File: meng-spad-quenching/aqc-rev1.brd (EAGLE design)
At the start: 127 x 88.9 mm, 138 parts, among them IC1 ADCMP582, IC2 NC7SV74K8X, IC3 LT3032-5, IC4 OPA342, IC5 OPA342, IC6 LTC1711, IC7 DS1100LU-20+, IC8 LT3032-15, IC9 NC7WZ16P6X, J1 VIN_LOGIC, M1 BSS806N, Q1 MMBTH81, Q2 MMBTH81, Q3 MMBTH81, Q4 MMBTH81, Q5 MMBTH81, Q6 MMBTH81, SW1 CJS-1200TB, SW2 CJS-1200TB, SW3 CJS-1200TB, T1 MMBTH10, T2 MMBTH10, T3 MMBTH10, T4 MMBTH10, T5 MMBTH10, T6 MMBTH10, T7 MMBTH10, U1 SN65EPT21DGK, U2 TPS78233DDCT, U3 SN65EPT22DGK, X1 CONN_SPAD, X2 CONN_PHOTON_COUNTER, X3 CONN_FORCE_QUENCH, X4 CONN_VREF_ONE_SHOT_EXT, X5 CONN_VREF_DIAMOND_IBIAS_EXT, X6 CONN_VREF_CASCODE_IBIAS_EXT

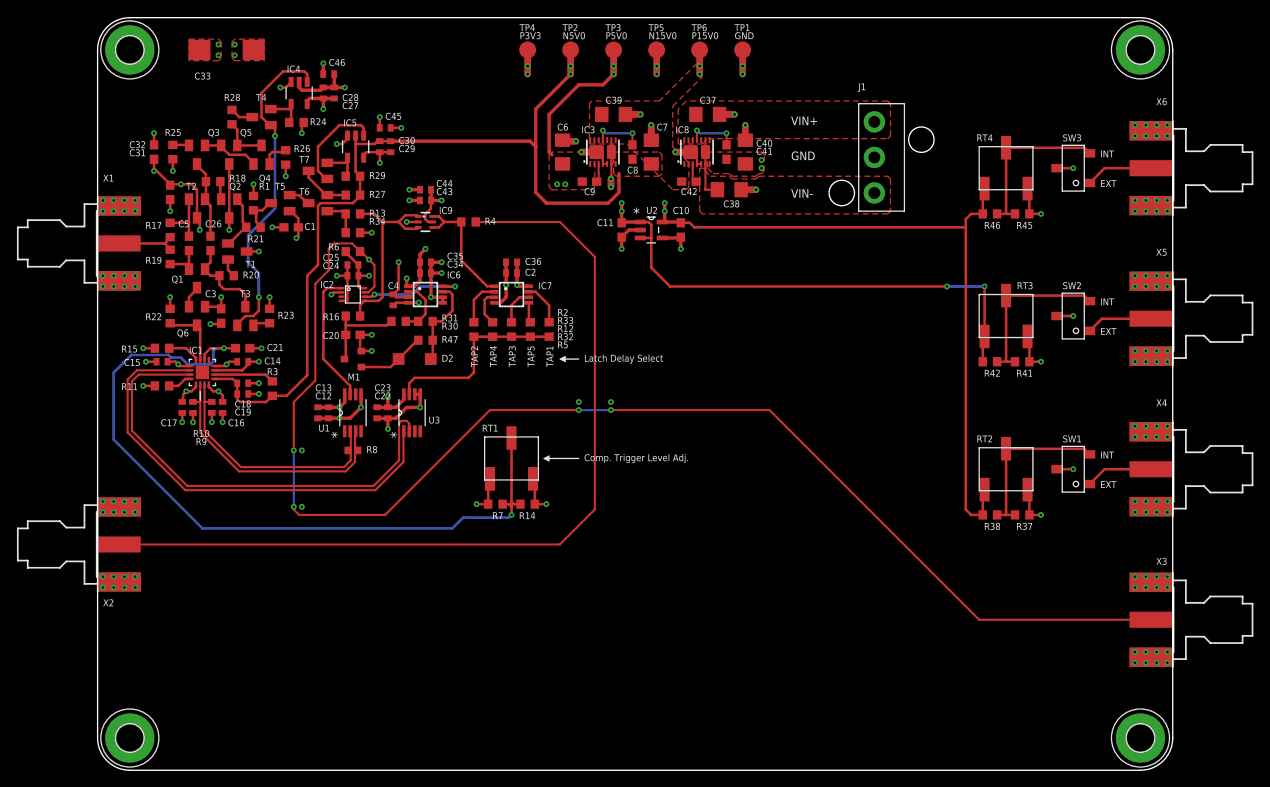
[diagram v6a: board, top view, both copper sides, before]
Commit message: Added VREF testpts, routed, exported gerbers
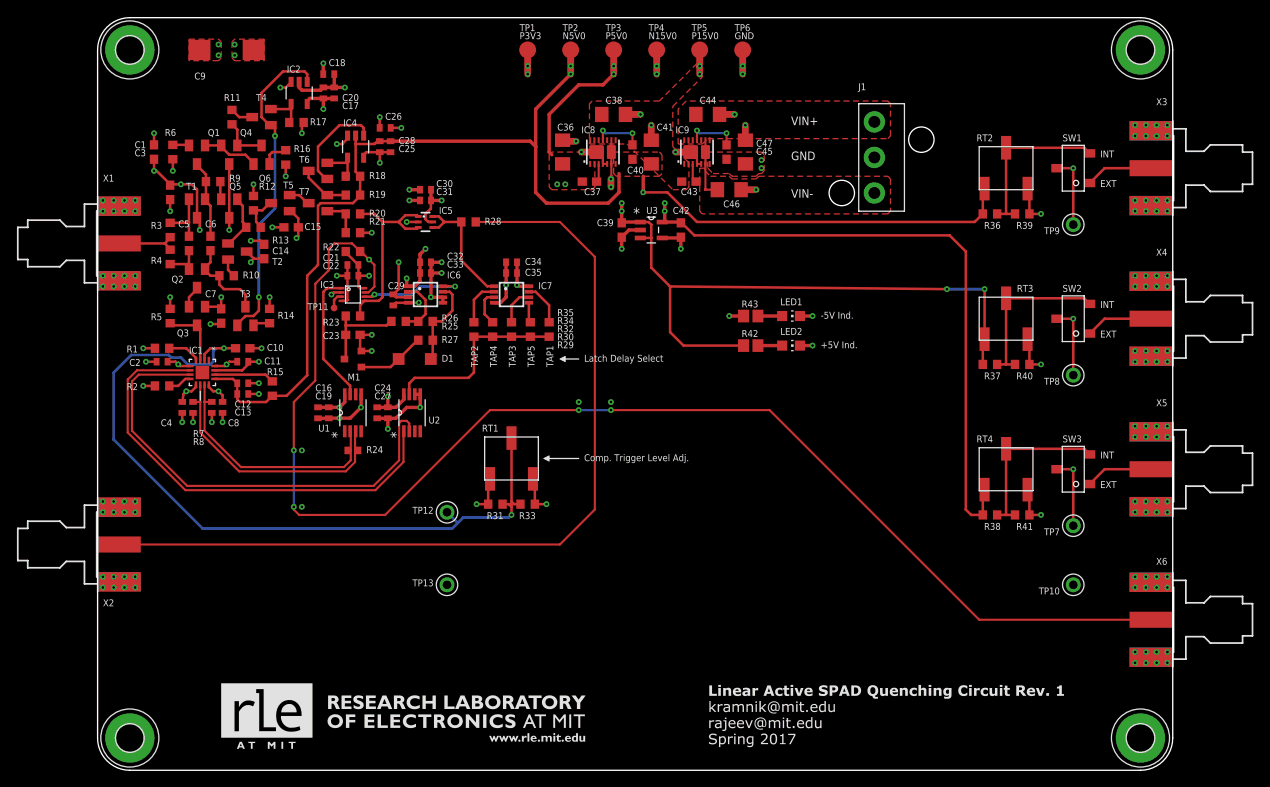
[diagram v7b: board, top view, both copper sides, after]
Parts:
- removed R47: 49R9, rcl:R0603
- added C47: 10u, rcl:C1206
- added LED1, LED2: (no value), led:CHIP-LED0805
- added R35, R40: DNP, rcl:R0603
- added R43: 470R, resistor:R0805
- added TP10, TP13: GND, Kramnik's Library:KEYSTONE_5000_MINIATURE
- added TP11: TPTP08R, testpad:TP08R
- added TP12: VREF_AV_DET, Kramnik's Library:KEYSTONE_5000_MINIATURE
- added TP7: VREF_ONE_SHOT, Kramnik's Library:KEYSTONE_5000_MINIATURE
- added TP8: VREF_DIAMOND_IBIAS, Kramnik's Library:KEYSTONE_5000_MINIATURE
- added TP9: VREF_CASCODE_IBIAS, Kramnik's Library:KEYSTONE_5000_MINIATURE
- C10, C16, C18, C25, C3, C35: value 100n -> 10n
- C11, C26, C31, C32: device rcl:C0603 -> rcl:C0402
- C14, C43, C45: device rcl:C0402 -> rcl:C0603
- C15: value 10n -> 100n; device rcl:C0402 -> rcl:C0603
- C19, C24, C34, C42: value 10n -> 100n
- C20: value 1n -> 100n; device rcl:C0603 -> rcl:C0402
- C21, C8: value 10n -> 100n; device rcl:C0603 -> rcl:C0402
- C23: value 100n -> 1n; device rcl:C0402 -> rcl:C0603
- C33: value 33u, 25V -> 10n; device rcl:CT7343 -> rcl:C0402
- C36, C44: value 100n -> 10u; device rcl:C0402 -> rcl:C1206
- C37, C40, C6: value 10u -> 10n; device rcl:C1206 -> rcl:C0603
- C39, C7: value 10u -> 100n; device rcl:C1206 -> rcl:C0603
- C41: value 10n -> 10u; device rcl:C0603 -> rcl:C1206
- C46: value 10n -> 10u; device rcl:C0402 -> rcl:C1206
- C9: value 10n -> 33u, 25V; device rcl:C0603 -> rcl:CT7343
- IC2: value NC7SV74K8X -> OPA342; device meng:US8_3.1MM_JDEC_MO-187 -> meng:SOT23-5
- IC3: value LT3032-5 -> NC7SV74K8X; device meng:DFN14-4X3DE -> meng:US8_3.1MM_JDEC_MO-187
- IC5: value OPA342 -> NC7WZ16P6X; device meng:SOT23-5 -> meng:SC70-6L
- IC8: value LT3032-15 -> LT3032-5
- IC9: value NC7WZ16P6X -> LT3032-15; device meng:SC70-6L -> meng:DFN14-4X3DE
- R1, R29: value 470R -> DNP
- R10, R9: value 150R -> 49R9; device rcl:R0402 -> rcl:R0603
- R11: value 49R9 -> 1k43
- R12: value DNP -> 470R
- R13: value 0R -> 49R9
- R14, R5: value DNP -> 1k
- R15: value DNP -> 10k
- R16: value 470R -> 1k
- R17, R6: value 49R9 -> 1k
- R18, R19: value 49R9 -> 470R
- R2: value DNP -> 49R9
- R20: value 49R9 -> 0R
- R21: value 49R9 -> DNP
- R22: value 1k -> 49R9
- R23: value 1k -> 470R
- R24: value 1k -> 100R; device rcl:R0603 -> rcl:R0402
- R25: value 1k -> 100R
- R26: value 1k -> 10k
- R27: value 470R -> 49R9
- R28: value 1k43 -> 49R9
- R3: value 10k -> 49R9
- R30: value 100R -> DNP
- R31: value 10k -> DNP
- R42: value DNP -> 470R; device rcl:R0603 -> resistor:R0805
- R7: value DNP -> 150R; device rcl:R0603 -> rcl:R0402
- R8: value 100R -> 150R
- U2: value TPS78233DDCT -> SN65EPT22DGK; device Texas Instruments_By_element14_Batch_1 (2):SOT95P280X110-5N -> Texas Instruments_By_element14_Batch_1:SOP65P490X110-8N
- U3: value SN65EPT22DGK -> TPS78233DDCT; device Texas Instruments_By_element14_Batch_1:SOP65P490X110-8N -> Texas Instruments_By_element14_Batch_1 (2):SOT95P280X110-5N
- X3: value CONN_FORCE_QUENCH -> CONN_VREF_CASCODE_IBIAS_EXT
- X4: value CONN_VREF_ONE_SHOT_EXT -> CONN_VREF_DIAMOND_IBIAS_EXT
- X5: value CONN_VREF_DIAMOND_IBIAS_EXT -> CONN_VREF_ONE_SHOT_EXT
- X6: value CONN_VREF_CASCODE_IBIAS_EXT -> CONN_FORCE_QUENCH
- moved H2 144.4 mm to (3.81, 3.81)
- moved H3 119.4 mm to (123.2, 85.1)
- moved H1 81.3 mm to (3.81, 85.1)
- moved C8 57.0 mm to (14.8, 42.9)
- moved C7 54.4 mm to (14.6, 53.7), turned to 270 degrees
- moved C10 53.6 mm to (17.1, 49.8), turned to 0 degrees
- moved X3 53.3 mm to (127.0, 71.1)
- moved X6 53.3 mm to (127.0, 17.8)
- moved C46 49.2 mm to (74.6, 68.6)
- moved C11 47.4 mm to (17.1, 48.3), turned to 0 degrees
- moved R2 46.2 mm to (7.62, 45.4), turned to 180 degrees
- moved C9 45.6 mm to (15.2, 85.1)
- moved C6 43.0 mm to (13.3, 62.2), turned to 270 degrees
- moved C2 42.6 mm to (7.62, 48.3)
- moved C17 40.7 mm to (26.7, 80.0), turned to 90 degrees
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- renumbered D2 to D1, R45 to R39, R46 to R36
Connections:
- new net N$39: LED1.A, R43.1
- new net N$40: LED2.A, R42.1
- net !FORCE_QUENCH: now also IC3.7, R22.1, X6.1; no longer IC2.7, R6.1, X3.1
- net !ONE_SHOT_CLR: now also IC3.6; no longer IC2.6
- net BLANKING_LATCH_EN: now also R29.1, R30.1, R34.1, R35.1, U2.7; no longer R12.1, R2.1, R33.1, R5.1, U3.7
- net COMP_LE_N: now also U2.1; no longer U3.1
- net COMP_LE_P: now also U2.2; no longer U3.2
- net COMP_Q_N: now also R24.1, R7.1; no longer R10.1, R8.1
- net COMP_Q_P: now also R24.2, R8.1; no longer R8.2, R9.1
- net GND: now also C26.2, C33.2, C41.2, C42.2, C47.2, C8.2, C9.-, IC2.2, IC4.5, IC5.2, IC9.4, IC9.5, LED2.C, Q4.C, R1.1, R17.1, R2.2, R21.2, R33.1, R40.2, R43.2, R5.1, R7.2, R8.2, TP10.P$1, TP13.P$1, TP6.TP, U2.5, U2.6, U3.2, U3.4; no longer C33.-, C37.2, C40.2, C43.2, C45.2, C6.2, IC2.4, IC3.5, IC4.2, IC5.5, IC9.2, Q2.C, R10.2, R11.2, R15.1, R22.1, R23.1, R24.1, R34.2, R37.2, R9.2, TP1.TP, U2.2, U2.4, U3.5, U3.6
- net HOLDOFF_TRIG: now also IC3.1; no longer IC2.1
- net LOGIC_QUENCH: now also IC3.5, IC5.1, IC5.3, R20.2, R23.2; no longer IC2.5, IC9.1, IC9.3, R13.2, R16.2
- net LOGIC_QUENCH_ATTEN: now also R20.1, R21.1, T7.B; no longer R13.1, R34.1, T6.B
- net N$1: now also R34.2; no longer R33.2
- net N$10: now also Q2.C, Q3.E; no longer Q1.C, Q6.E
- net N$11: now also Q5.E, R9.1; no longer Q2.E, R18.1
- net N$12: now also C6.1, Q1.C, R9.2, T1.B; no longer C26.1, Q3.C, R18.2, T2.B
- net N$13: now also R10.2, T2.E; no longer R20.2, T1.E
- net N$14: now also Q2.E, R4.1; no longer Q1.E, R19.1
- net N$15: now also T7.C; no longer T6.C
- net N$16: now also IC2.1; no longer IC4.1
- net N$17: now also R32.2; no longer R12.2
- net N$18: now also Q4.B, Q6.C, R11.2; no longer Q4.C, Q5.B, R28.2
- net N$19: now also C6.2, Q2.B, R10.1; no longer C26.2, Q1.B, R20.1
- net N$2: now also R28.1; no longer R4.1
- net N$20: now also R14.2; no longer R23.2
- net N$21: now also Q5.B, R13.1, T2.B; no longer Q2.B, R21.1, T1.B
- net N$22: now also R12.1, R13.2; no longer R1.1, R21.2
- net N$23: now also IC2.4, R17.2; no longer IC4.4, R24.2
- net N$24: now also R19.2, T6.C, T7.E; no longer R27.2, T6.E, T7.C
- net N$25: now also R25.1, R26.2; no longer R30.1, R31.2
- net N$26: now also Q1.E, R6.1; no longer Q3.E, R25.1
- net N$27: now also R11.1; no longer R28.1
- net N$28: now also R29.2; no longer R5.2
- net N$29: now also Q6.E, R16.1; no longer Q4.E, R26.1
- net N$3: now also R1.2; no longer R15.2
- net N$30: now also IC4.1, T6.B; no longer IC5.1, T7.B
- net N$31: now also Q1.B, Q4.E, Q6.B; no longer Q3.B, Q4.B, Q5.E
- net N$32: now also R35.2; no longer R2.2
- net N$33: now also C43.1, IC9.3; no longer C42.1, IC8.3
- net N$34: now also C45.1, IC9.11; no longer C41.1, IC8.11
- net N$35: now also IC4.4, R18.2, T6.E; no longer IC5.4, R29.2, T7.E
- net N$36: now also R27.2; no longer R47.2
- net N$37: now also IC5.4, IC5.6, R28.2; no longer IC9.4, IC9.6, R4.2
- net N$4: now also R15.2; no longer R3.2
- net N$5: now also R3.2, T1.E; no longer R17.2, T2.E
- net N$6: now also R2.1; no longer R11.1
- net N$7: now also R30.2; no longer R32.2
- net N$8: now also C37.1, IC8.3; no longer C9.1, IC3.3
- net N$9: now also C40.1, IC8.11; no longer C8.1, IC3.11
- net NC_!LOGIC_QUENCH: now also IC3.3, TP11.TP; no longer IC2.3
- net ONE_SHOT_CAP: now also C23.1, R23.1, R25.2; no longer C20.1, R16.1, R30.2
- net ONE_SHOT_CLR: now also R26.1, R27.1; no longer R31.1, R47.1
- net PP_N15V0: now also C45.2, C47.1, IC8.6, IC8.9, IC9.7, TP4.TP; no longer C40.1, C41.2, IC3.6, IC3.9, IC8.7, TP5.TP
- net PP_N5V0: now also C12.1, C13.1, C25.1, C28.1, C40.2, C41.1, IC4.2, IC8.7, LED1.C, R15.1, R18.1, R19.1, R36.1, RT2.1; no longer C18.1, C19.1, C29.1, C30.1, C7.1, C8.2, IC3.7, IC5.2, R27.1, R29.1, R3.1
- net PP_NVIN: now also C46.1, IC9.6, IC9.9; no longer C38.1, IC8.6, IC8.9
- net PP_P15V0: now also C1.1, C14.1, C3.1, C38.1, C43.2, C9.+, IC8.10, IC8.12, IC8.14, IC9.1, R12.2, R16.2, R6.2, TP5.TP; no longer C31.1, C32.1, C33.+, C39.1, C42.2, IC3.10, IC3.12, IC3.14, IC8.1, R1.2, R25.2, R26.2, TP6.TP
- net PP_P3V3: now also C19.1, C21.1, C27.1, C30.1, C31.1, C32.1, C33.1, C4.1, C42.1, C8.1, IC3.2, IC3.8, IC5.5, R22.2, TP1.TP, U2.8, U3.5; no longer C10.1, C12.1, C13.1, C17.1, C2.1, C23.1, C25.1, C36.1, C43.1, C44.1, IC2.2, IC2.8, IC9.5, R36.1, R6.2, RT2.1, TP4.TP, U2.5, U3.8
- net PP_P5V0: now also C17.1, C2.1, C20.1, C36.1, C37.2, C39.1, C7.1, IC2.5, IC8.1, Q3.B, R31.2, R37.1, R42.2, U3.1, U3.3; no longer C1.1, C14.1, C27.1, C28.1, C3.1, C6.1, C9.2, IC3.1, IC4.5, Q6.B, R42.1, R7.2, U2.1, U2.3
- net PP_PVIN: now also C44.1, IC9.10, IC9.12, IC9.14; no longer C37.1, IC8.10, IC8.12, IC8.14
- net SPAD_PULLDN_SENSE: now also Q3.C, R5.2; no longer Q6.C, R22.2
- net VREF_AV_DET: now also C10.1, R31.1, R33.2, TP12.P$1; no longer C21.1, R14.2, R7.1
- net VREF_CASCODE_IBIAS: now also C26.1, IC4.3, SW1.2, TP9.P$1; no longer C45.1, IC5.3, SW3.2
- net VREF_CASCODE_IBIAS_EXT: now also SW1.1, X3.1; no longer SW3.1, X6.1
- net VREF_CASCODE_IBIAS_INT: now also RT2.2, SW1.3; no longer RT4.2, SW3.3
- net VREF_DIAMOND_IBIAS: now also C18.1, IC2.3, TP8.P$1; no longer C46.1, IC4.3
- net VREF_DIAMOND_IBIAS_EXT: now also X4.1; no longer X5.1
- net VREF_DIAMOND_IBIAS_INT: now also R37.2, R40.1; no longer R41.1, R42.2
- net VREF_ONE_SHOT: now also C29.1, SW3.2, TP7.P$1; no longer C4.1, SW1.2
- net VREF_ONE_SHOT_EXT: now also SW3.1, X5.1; no longer SW1.1, X4.1
- net VREF_ONE_SHOT_INT: now also R41.1, RT4.2, SW3.3; no longer R37.1, RT2.2, SW1.3
- net VSPAD: now also R3.1, R4.2; no longer R17.1, R19.2
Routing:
- net PP_N5V0: track 102.3 -> 176.8 mm, vias 2 -> 4
- net PP_P5V0: track 262.2 -> 276.9 mm
- net VREF_DIAMOND_IBIAS: track 132.8 -> 140.8 mm
- net PP_P3V3: track 241.1 -> 233.1 mm
- net VREF_ONE_SHOT: track 102.4 -> 109.1 mm
- net VREF_CASCODE_IBIAS: track 109.5 -> 115.0 mm
- net GND: track 170.3 -> 175.2 mm, vias 156 -> 159
- net N$40: track 0.00 -> 2.86 mm
- net N$39: track 0.00 -> 2.86 mm
- net NC_!LOGIC_QUENCH: track 0.00 -> 1.98 mm
- net VREF_AV_DET: track 91.9 -> 93.7 mm
- net PP_P15V0: track 73.2 -> 74.8 mm
- net N$16: track 39.2 -> 38.2 mm
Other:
- board text added: "+5V Ind."
- board text added: "-5V Ind."

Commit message: Renumbered, moved some refdes, checked and approved all DRC violations, exported gerbers
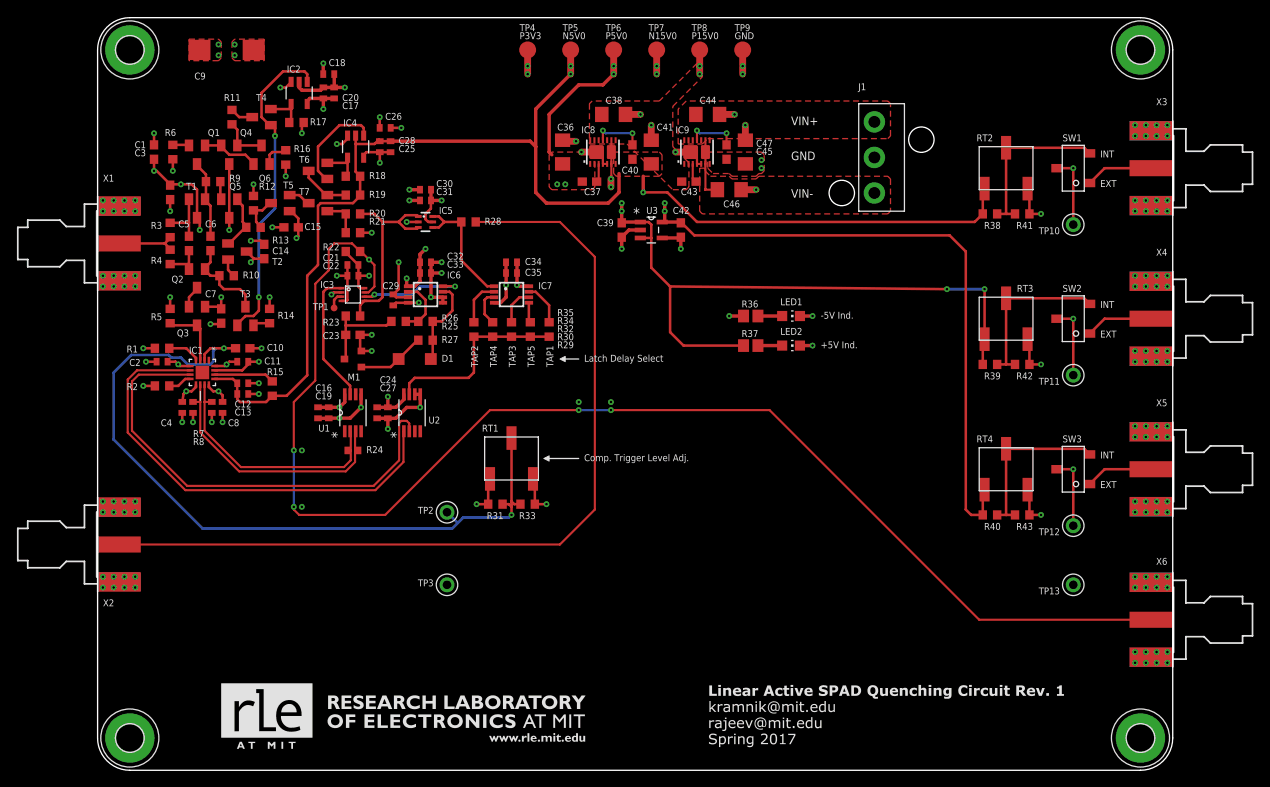
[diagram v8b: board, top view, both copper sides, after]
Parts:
- R36, R37: value DNP -> 470R; device rcl:R0603 -> resistor:R0805
- R42, R43: value 470R -> DNP; device resistor:R0805 -> rcl:R0603
- TP1: value TPTP20R -> TPTP08R; device testpad:TP20R -> testpad:TP08R
- TP10: value GND -> VREF_CASCODE_IBIAS
- TP11: value TPTP08R -> VREF_DIAMOND_IBIAS; device testpad:TP08R -> Kramnik's Library:KEYSTONE_5000_MINIATURE
- TP12: value VREF_AV_DET -> VREF_ONE_SHOT
- TP2: value TPTP20R -> VREF_AV_DET; device testpad:TP20R -> Kramnik's Library:KEYSTONE_5000_MINIATURE
- TP3: value TPTP20R -> GND; device testpad:TP20R -> Kramnik's Library:KEYSTONE_5000_MINIATURE
- TP7: value VREF_ONE_SHOT -> TPTP20R; device Kramnik's Library:KEYSTONE_5000_MINIATURE -> testpad:TP20R
- TP8: value VREF_DIAMOND_IBIAS -> TPTP20R; device Kramnik's Library:KEYSTONE_5000_MINIATURE -> testpad:TP20R
- TP9: value VREF_CASCODE_IBIAS -> TPTP20R; device Kramnik's Library:KEYSTONE_5000_MINIATURE -> testpad:TP20R
- moved TP11 87.7 mm to (115.3, 46.7)
- moved TP7 74.7 mm to (66.0, 85.1)
- moved TP12 74.0 mm to (115.3, 28.9)
- moved TP13 74.0 mm to (115.3, 21.9)
- moved TP3 66.2 mm to (41.3, 21.9)
- moved TP8 58.5 mm to (71.1, 85.1)
- moved TP2 56.5 mm to (41.3, 30.5)
- moved TP9 44.2 mm to (76.2, 85.1)
- moved TP10 42.5 mm to (115.3, 64.5)
- moved R43 39.8 mm to (109.2, 30.2), turned to 0 degrees
- moved TP1 38.1 mm to (27.9, 54.6)
- moved R38 35.6 mm to (105.4, 65.7)
- moved R41 35.6 mm to (109.2, 65.7)
- moved R42 32.1 mm to (109.2, 47.9), turned to 0 degrees
- moved R36 30.7 mm to (77.2, 53.7), turned to 180 degrees
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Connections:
- net GND: now also R36.2, R42.2, TP3.P$1, TP9.TP; no longer R39.2, R40.2, TP10.P$1, TP6.TP
- net N$39: now also R36.1; no longer R43.1
- net N$40: now also R37.1; no longer R42.1
- net NC_!LOGIC_QUENCH: now also TP1.TP; no longer TP11.TP
- net PP_N15V0: now also TP7.TP; no longer TP4.TP
- net PP_N5V0: now also R38.1, TP5.TP; no longer R36.1, TP2.TP
- net PP_P15V0: now also TP8.TP; no longer TP5.TP
- net PP_P3V3: now also R40.1, TP4.TP; no longer R38.1, TP1.TP
- net PP_P5V0: now also R37.2, R39.1, TP6.TP; no longer R37.1, R42.2, TP3.TP
- net VREF_AV_DET: now also TP2.P$1; no longer TP12.P$1
- net VREF_CASCODE_IBIAS: now also TP10.P$1; no longer TP9.P$1
- net VREF_CASCODE_IBIAS_INT: now also R38.2, R41.1; no longer R36.2, R39.1
- net VREF_DIAMOND_IBIAS: now also TP11.P$1; no longer TP8.P$1
- net VREF_DIAMOND_IBIAS_INT: now also R39.2, R42.1; no longer R37.2, R40.1
- net VREF_ONE_SHOT: now also TP12.P$1; no longer TP7.P$1
- net VREF_ONE_SHOT_INT: now also R40.2, R43.1; no longer R38.2, R41.1
